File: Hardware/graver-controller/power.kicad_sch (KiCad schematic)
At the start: 36 parts, among them J101 DC jack 5.5x2.1, Q101 DMP6023LE, U101 LM5164DDAR, U102 AP2112K-3.3

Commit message: hardware: design rules and net classes in the project, U101 without library thermal vias
Board minimums 0.2 mm track, 0.15 mm clearance, 0.6/0.3 mm via, 0.3 mm
copper to edge; net classes Default 0.2, Power 0.5 (+3V3, +5V, VBUS,
VDDA), HighCurrent 0.8 / 0.4 mm clearance (VIN, COIL_NEG, CLAMP,
SHUNT_HI). The HSOP-8 ThermalVias footprint carries 0.2 mm drills, below
the board minimum; the EP vias get added by the copper script instead.
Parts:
- U101: footprint Package_SO:HSOP-8-1EP_3.9x4.9mm_P1.27mm_EP2.41x3.1mm_ThermalVias -> Package_SO:HSOP-8-1EP_3.9x4.9mm_P1.27mm_EP2.41x3.1mm
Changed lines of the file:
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@@
 			)
 		)
-		(property "Footprint" "Package_SO:HSOP-8-1EP_3.9x4.9mm_P1.27mm_EP2.41x3.1mm_ThermalVias"
+		(property "Footprint" "Package_SO:HSOP-8-1EP_3.9x4.9mm_P1.27mm_EP2.41x3.1mm"
 			(at 133.35 173.99 0)
 			(hide yes)

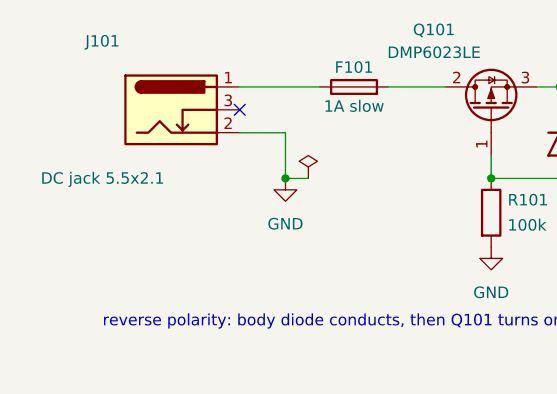
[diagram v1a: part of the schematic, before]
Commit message: hardware: wire pads instead of connectors, board to 95 x 70
ADR 0003 Decision 9. Every board connector except USB-C becomes a row of
plated through-holes and the rotary encoder moves off the board onto wires;
Jan solders the looms at box build. The mating halves were the sourcing
problem, not the board halves, and the four connectors dropped here were
also the four parts whose footprints were still unverified against real
hardware.

Schematic (ERC 0, netlist diffed pad-by-pad - every difference was an
auto-generated net NAME following its anchor pin, no connectivity changed):

- J101 Barrel_Jack_Switch -> Conn_01x02, SolderWire-1sqmm 1x02, 1.4 mm
- J201 -> PinHeader_1x04, J401 -> PinHeader_1x07
- J402 AudioJack3_SwitchTR -> Conn_01x04 (TIP, RN, RING, SLV)
- SW401 RotaryEncoder_Switch_MP -> J403 Conn_01x04 (A, GND, B, SW)
- the five pad rows carry no LCSC/MPN: they are holes, not parts, and an
  empty field reads as a schematic-parity mismatch
- three orphaned no-connect flags removed with the old unused pins

Board 110 x 70 -> 95 x 70: measured on the routed board, everything except
the connectors, the encoder and the mounting holes fits in 84.5 x 64.0 mm,
so the connectors were setting the width. 95 also brings the long side
under JLC's 100 x 100 price band.

State: 0 DRC errors, 0 schematic parity, 3 unconnected pad pairs (+5V and
two GND, all short same-net gaps), 11 warnings, 126 vias, all placement
checks and ADR criteria PASS, all eight per-net width floors PASS.

Tooling:

- outline 95 x 70 in place.py, copper.py, silk.py and render.sh
- rear pad rows inset from the edge (negative overhang): J101's 2.7 mm pads
  sitting flush broke the 0.3 mm copper-to-edge rule
- silk legends rewritten; the two MIDDLE pads of each 1x4 rear row had no
  sideways escape at 2.54 mm pitch and silently got no label, which on the
  handpiece row is 24 V versus the NTC input. Pin numbers dropped and the
  seed pushed to 3.6 mm; 24 of 24 legends now place on seed.
- copper.py BRIDGE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
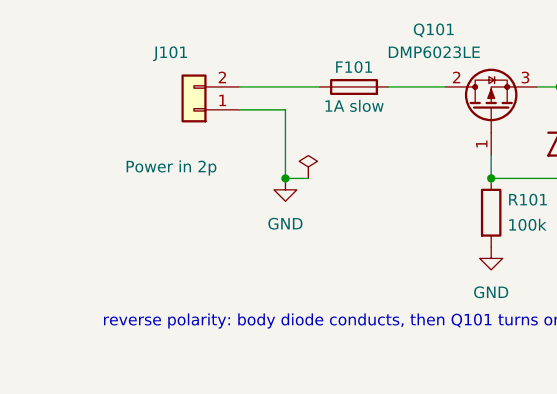
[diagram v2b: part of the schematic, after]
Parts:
- removed J101: DC jack 5.5x2.1, Connector_BarrelJack:BarrelJack_Horizontal, symbol Connector:Barrel_Jack_Switch
- added J101: Power in 2p, Connector_Wire:SolderWire-1sqmm_1x02_P5.4mm_D1.4mm_OD2.7mm, symbol Connector_Generic:Conn_01x02
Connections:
- net GND: now also J101.1 (Pin_1)
- net at F101.1: now also J101.2 (Pin_2)
- no-connect marks 3 -> 2
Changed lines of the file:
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@@
 	)
 	(no_connect
-		(at 68.58 106.68)
-	)
-	(no_connect
 		(at 146.05 179.07)
 	)
@@
 	(wire
 		(pts
-			(xy 68.58 109.22) (xy 73.66 109.22)
-		)
-		(stroke
-			(width 0)
-			(type default)
-		)
-	)
-	(wire
-		(pts
 			(xy 146.05 166.37) (xy 149.86 166.37)
 		)
@@
 	)
 	(symbol
-		(lib_id "Connector:Barrel_Jack_Switch")
-		(at 60.96 106.68 0)
+		(lib_id "Connector_Generic:Conn_01x02")
+		(at 63.5 106.68 180)
 		(unit 1)
 		(body_style 1)
@@
 		(dnp no)
 		(property "Reference" "J101"
-			(at 53.34 99.06 0)
+			(at 60.96 100.33000000000001 0)
 			(show_name no)
 			(do_not_autoplace no)
@@
 			)
 		)
-		(property "Value" "DC jack 5.5x2.1"
-			(at 53.34 114.3 0)
+		(property "Value" "Power in 2p"
+			(at 60.96 113.03 0)
 			(show_name no)
 			(do_not_autoplace no)
@@
 			)
 		)
-		(property "Footprint" "Connector_BarrelJack:BarrelJack_Horizontal"
-			(at 60.96 106.68 0)
+		(property "Footprint" "Connector_Wire:SolderWire-1sqmm_1x02_P5.4mm_D1.4mm_OD2.7mm"
+			(at 63.5 106.68 0)
 			(hide yes)
 			(show_name no)
@@
 		)
 		(property "Datasheet" ""
-			(at 60.96 106.68 0)
+			(at 63.5 106.68 0)
 			(hide yes)
 			(show_name no)
@@
 		)
 		(property "Description" ""
-			(at 60.96 106.68 0)
-			(hide yes)
-			(show_name no)
-			(do_not_autoplace no)
-			(effects
-				(font
-					(size 1.27 1.27)
-				)
-			)
-		)
-		(property "LCSC" "C720557"
-			(at 60.96 106.68 0)
-			(hide yes)
-			(show_name no)
-			(do_not_autoplace no)
-			(effects
-				(font
-					(size 1.27 1.27)
-				)
-			)
-		)
-		(property "MPN" "DC-005-A200"
-			(at 60.96 106.68 0)
+			(at 63.5 106.68 0)
 			(hide yes)
 			(show_name no)
@@
 		(pin "2"
 		)
-		(pin "3"
-		)
 		(instances
 			(project "graver-controller"
@@
 		)
 	)
+	(wire
+		(pts
+			(xy 68.58 106.68) (xy 73.66 106.68)
+		)
+		(stroke
+			(width 0)
+			(type default)
+		)
+	)
+	(wire
+		(pts
+			(xy 73.66 106.68) (xy 73.66 109.22)
+		)
+		(stroke
+			(width 0)
+			(type default)
+		)
+	)

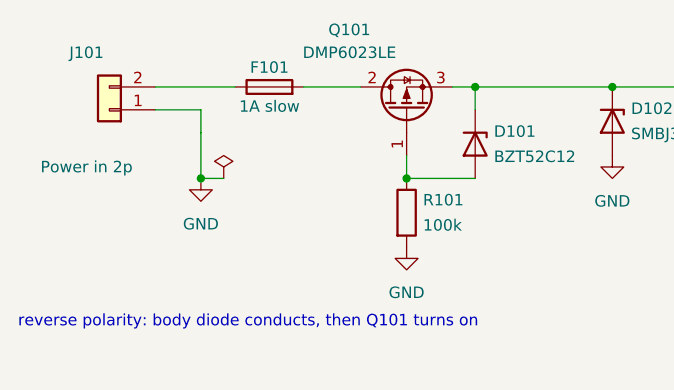
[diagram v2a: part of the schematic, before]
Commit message: graver pcb: F101 -> 1206L035/30WR PTC; the 0437001.WR is a fast fuse and blows on hot-plug inrush
Board 1 blew F101 on the first 24 V connect. The 437 series is fast-acting
(1 A, I2t 0.100 A2s), not Slo-Blo as the parts doc said; hot-plugging 24 V
into C101 470 uF is roughly 0.27-0.45 A2s. A 1206 PTC (0.35 A hold, 30 V,
Imax 100 A) ignores the inrush pulse and resets after a fault. Same footprint,
so the 12 built boards take it as a one-part swap. fab/ is left as built.
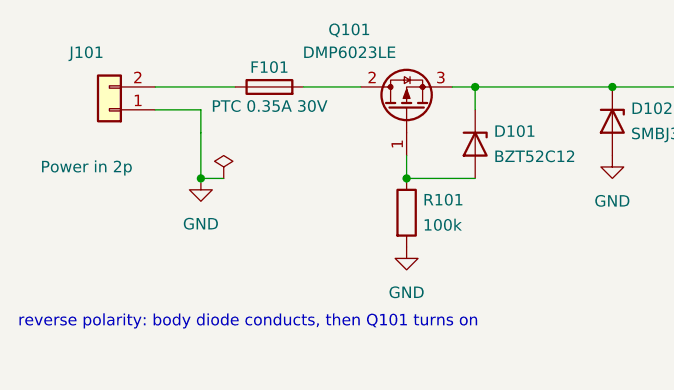
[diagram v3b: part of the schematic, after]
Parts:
- F101: value 1A slow -> PTC 0.35A 30V; LCSC C99537 -> C2153989; MPN 0437001.WR -> 1206L035/30WR
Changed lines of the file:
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@@
 			)
 		)
-		(property "Value" "1A slow"
+		(property "Value" "PTC 0.35A 30V"
 			(at 81.28 106.302 270)
 			(show_name no)
@@
 			)
 		)
-		(property "Description" ""
+		(property "Description" "Resettable PTC, 0.35 A hold / 0.75 A trip, 30 V, Imax 100 A; survives hot-plug inrush into C101"
 			(at 81.28 104.14 0)
 			(hide yes)
@@
 			)
 		)
-		(property "LCSC" "C99537"
+		(property "LCSC" "C2153989"
 			(at 81.28 104.14 0)
 			(hide yes)
@@
 			)
 		)
-		(property "MPN" "0437001.WR"
+		(property "MPN" "1206L035/30WR"
 			(at 81.28 104.14 0)
 			(hide yes)

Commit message: power sch: U103 TPS26602 eFuse replaces F101/Q101/D101/R101 (ADR 0007)
IN = J101 +24V with C117 100nF 100V and R111 100k to SHDN; OUT = VIN.
UVLO/OVP/MODE, ILIM (R112 12k 1%, basic part, 1.0 A) and dVdT (C116
220nF, 42 ms) return to the new RTN net. VIN PWR_FLAG moved to the IN
net (U103 OUT drives VIN). J101 group shifted 20.32 mm left. ERC 0.
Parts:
- removed D101: BZT52C12, Diode_SMD:D_SOD-123, symbol Device:D_Zener
- removed F101: PTC 0.35A 30V, Fuse:Fuse_1206_3216Metric, symbol Device:Fuse
- removed Q101: DMP6023LE, Package_TO_SOT_SMD:SOT-223-3_TabPin2, symbol Transistor_FET:Q_PMOS_GDS
- removed R101: 100k, Resistor_SMD:R_0603_1608Metric, symbol Device:R
- added C116: 220nF, Capacitor_SMD:C_0603_1608Metric, symbol Device:C
- added C117: 100nF 100V, Capacitor_SMD:C_0805_2012Metric, symbol Device:C
- added R111: 100k, Resistor_SMD:R_0603_1608Metric, symbol Device:R
- added R112: 12k 1%, Resistor_SMD:R_0603_1608Metric, symbol Device:R
- added U103: TPS26602PWPR, Package_SO:HTSSOP-16-1EP_4.4x5mm_P0.65mm_EP3.4x5mm_Mask3x3mm_ThermalVias, symbol Power_Management:TPS26602PWP
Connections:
- net GND: now also C117.2, U103.9 (GND)
- net VIN: now also U103.15 (OUT), U103.16 (OUT)
- net at J101.2 (Pin_2): now also C117.1, R111.1, U103.1 (IN), U103.2 (IN)
- new net: R112.1, U103.11 (ILIM)
- new net: C116.1, U103.12 (dVdT)
- new net: R111.2, U103.7 (~{SHDN})
- new net RTN: C116.2, R112.2, U103.17 (RTN), U103.3 (UVLO), U103.5 (OVP), U103.6 (MODE), U103.8 (RTN)
- no-connect marks 2 -> 4
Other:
- note added: "U103 eFuse (ADR 0007): reverse polarity, 1.0 A limit with auto-retry (R112), 42 ms soft start (C116), UVLO 14.9 V, 38 V clamp. RTN is its own net and copper island: never tie it to GND."
- note removed: "reverse polarity: body diode conducts, then Q101 turns on"
- moved on the sheet: J101
